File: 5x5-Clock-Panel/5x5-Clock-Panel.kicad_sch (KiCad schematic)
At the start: 0 parts

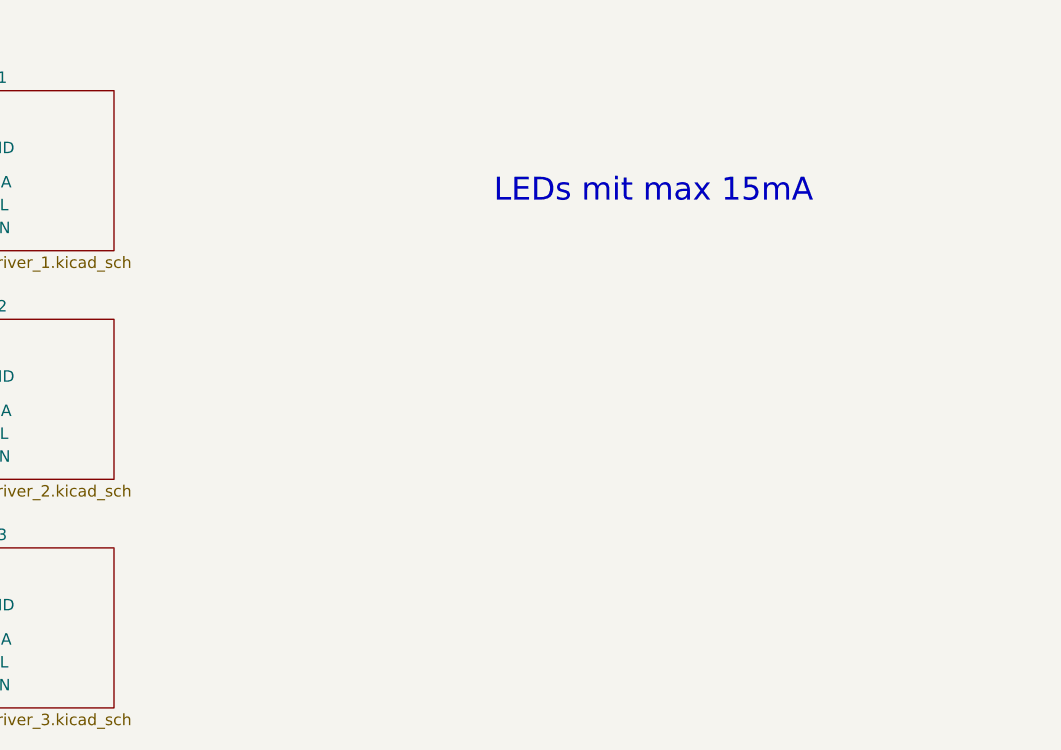
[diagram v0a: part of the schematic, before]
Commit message: Assigned LEDs to LED-Drivers in the concept.
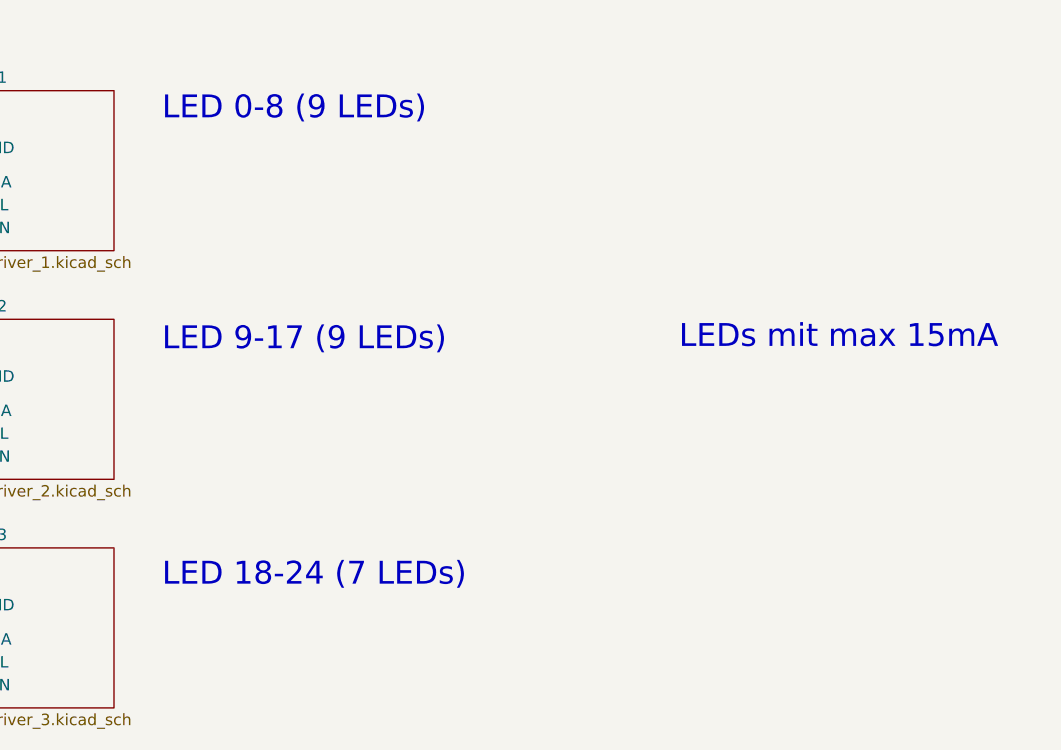
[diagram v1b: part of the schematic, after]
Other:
- note added: "LED 0-8 (9 LEDs)"
- note added: "LED 18-24 (7 LEDs)"
- note added: "LED 9-17 (9 LEDs)"
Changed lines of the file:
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@@
+		)
+	)
+	(text "LED 0-8 (9 LEDs)"
+		(exclude_from_sim no)
+		(at 284.734 103.632 0)
+		(effects
+			(font
+				(size 2.54 2.54)
+			)
+			(justify left)
 		)
 	)
 	(text "LEDs mit max 15mA"
 		(exclude_from_sim no)
-		(at 339.344 112.776 0)
+		(at 359.918 129.032 0)
 		(effects
 			(font
@@
 		)
 	)
+	(text "LED 18-24 (7 LEDs)\n"
+		(exclude_from_sim no)
+		(at 284.734 155.448 0)
+		(effects
+			(font
+				(size 2.54 2.54)
+			)
+			(justify left)
+		)
+	)
+	(text "LED 9-17 (9 LEDs)"
+		(exclude_from_sim no)
+		(at 284.734 129.286 0)
+		(effects
+			(font
+				(size 2.54 2.54)
+			)
+			(justify left)
+		)
+	)
